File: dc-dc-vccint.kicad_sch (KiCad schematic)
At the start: 53 parts, among them U36 MP8796B, U37 MP8796B

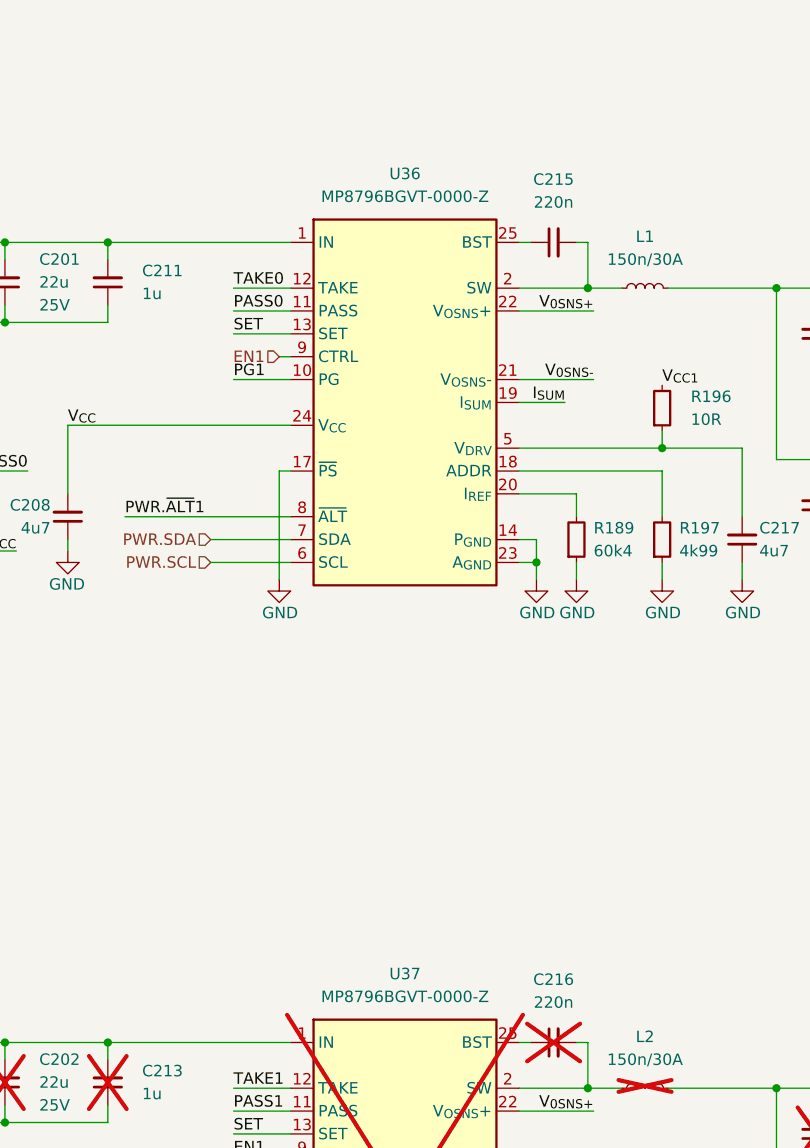
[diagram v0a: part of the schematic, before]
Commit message: [#66727] Update legacy footprints
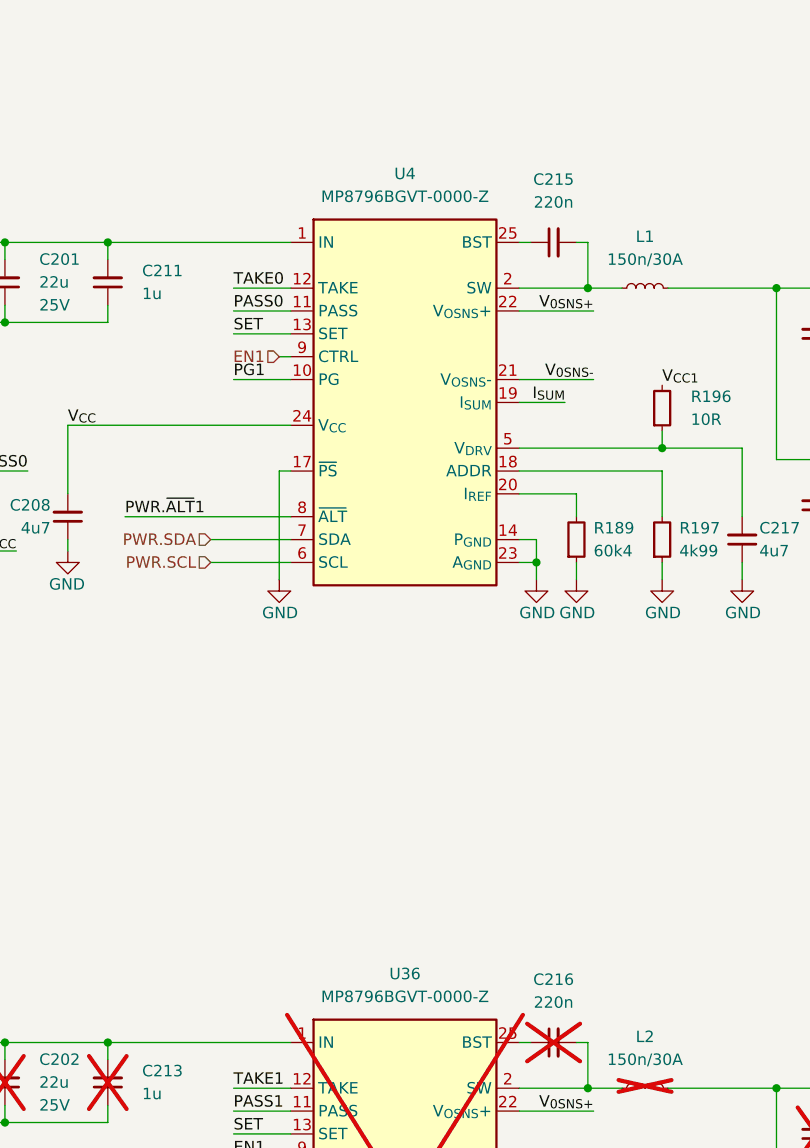
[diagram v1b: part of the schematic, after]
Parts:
- removed U36, U37: MP8796B, symbol antmicroDCDCConverters:MP8796B
- added U36, U4: MP8796B, antmicro-footprints:TQFN-25_4x5mm, symbol DCDCConverters:MP8796B
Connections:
- net EN1: now also U36.9 (CTRL), U4.9 (CTRL)
- net GND: now also U36.14 (P_{GND}), U36.15 (P_{GND}), U36.23 (A_{GND}), U36.4 (P_{GND}), U4.14 (P_{GND}), U4.15 (P_{GND}), U4.17 (~{PS}), U4.23 (A_{GND}), U4.4 (P_{GND})
- net I_{SUM}: now also U36.19 (I_{SUM}), U4.19 (I_{SUM})
- net PASS0: now also U4.11 (PASS)
- net PASS1: now also U36.11 (PASS)
- net PG1: now also U36.10 (PG), U4.10 (PG)
- net PWR.SCL: now also U36.6 (SCL), U4.6 (SCL)
- net PWR.SDA: now also U36.7 (SDA), U4.7 (SDA)
- net PWR.~{ALT}1: now also U4.8 (~{ALT})
- net PWR.~{ALT}2: now also U36.8 (~{ALT})
- net SET: now also U36.13 (SET), U4.13 (SET)
- net TAKE0: now also U4.12 (TAKE)
- net TAKE1: now also U36.12 (TAKE)
- net VDC: now also U36.1 (IN), U36.16 (IN), U4.1 (IN), U4.16 (IN)
- net V_{0SNS+}: now also U36.22 (V_{OSNS}+), U4.22 (V_{OSNS}+)
- net V_{0SNS-}: now also U36.21 (V_{OSNS}-), U4.21 (V_{OSNS}-)
- net V_{CC}: now also U36.24 (V_{CC}), U4.24 (V_{CC})
- net at C218.2, R198.1: now also U36.5 (V_{DRV})
- net at R189.2: now also U4.20 (I_{REF})
- net at R199.2: now also U36.18 (ADDR)
- net at C216.2, L2.1: now also U36.2 (SW), U36.3 (SW)
- net at R195.2: now also U36.20 (I_{REF})
- net at C216.1: now also U36.25 (BST)
- net at C217.2, R196.1: now also U4.5 (V_{DRV})
- net at R197.2: now also U4.18 (ADDR)
- net at C215.1: now also U4.25 (BST)
- net at C215.2, L1.1: now also U4.2 (SW), U4.3 (SW)
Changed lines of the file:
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@@
-    )
-  )
-  (symbol (lib_id "antmicroDCDCConverters:MP8796B") (at 177.8 152.4 0) (unit 1)
-    (in_bom yes) (on_board yes) (dnp yes) (fields_autoplaced)
-    (property "Reference" "U37" (at 190.5 144.78 0)
-      (effects (font (size 1.27 1.27) (thickness 0.15)))
-    )
-    (property "Value" "MP8796B" (at 215.9 162.56 0)
-      (effects (font (size 1.27 1.27) (thickness 0.15)) (justify left bottom) hide)
-    )
-    (property "Footprint" "" (at 215.9 165.1 0)
-      (effects (font (size 1.27 1.27) (thickness 0.15)) (justify left bottom) hide)
-    )
-    (property "Datasheet" "https://www.monolithicpower.com/en/documentview/productdocument/index/version/2/document_type/Datasheet/lang/en/sku/MP8796B/" (at 215.9 167.64 0)
-      (effects (font (size 1.27 1.27) (thickness 0.15)) (justify left bottom) hide)
-    )
-    (property "MPN" "MP8796BGVT-0000-Z" (at 190.5 147.32 0)
-      (effects (font (size 1.27 1.27) (thickness 0.15)))
-    )
-    (property "Manufacturer" "Monolithic Power Systems" (at 215.9 160.02 0)
-      (effects (font (size 1.27 1.27) (thickness 0.15)) (justify left bottom) hide)
-    )
-    (property "Author" "Antmicro" (at 215.9 170.18 0)
-      (effects (font (size 1.27 1.27) (thickness 0.15)) (justify left bottom) hide)
-    )
-    (property "License" "Apache-2.0" (at 215.9 172.72 0)
-      (effects (font (size 1.27 1.27) (thickness 0.15)) (justify left bottom) hide)
-    )
-    (pin "13")
-    (pin "16")
-    (pin "14")
-    (pin "24")
-    (pin "6")
-    (pin "23")
-    (pin "21")
-    (pin "17")
-    (pin "10")
-    (pin "18")
-    (pin "8")
-    (pin "7")
-    (pin "9")
-    (pin "25")
-    (pin "15")
-    (pin "4")
-    (pin "19")
-    (pin "12")
-    (pin "20")
-    (pin "3")
-    (pin "1")
-    (pin "11")
-    (pin "22")
-    (pin "5")
-    (pin "2")
-    (instances
-      (project "data-center-rdimm-ddr5-tester"
-        (path "/1faa6543-e26a-4449-8bac-ee14b9f19e5f/00000000-0000-0000-0000-000060225b0c/3cfc3a6a-24b0-4207-8c35-05eeccc29696"
-          (reference "U37") (unit 1)
-        )
-      )
     )
   )
@@
         (path "/1faa6543-e26a-4449-8bac-ee14b9f19e5f/00000000-0000-0000-0000-000060225b0c/3cfc3a6a-24b0-4207-8c35-05eeccc29696"
           (reference "#PWR0456") (unit 1)
+        )
+      )
+    )
+  )
+  (symbol (lib_id "DCDCConverters:MP8796B") (at 177.8 63.5 0) (unit 1)
+    (in_bom yes) (on_board yes) (dnp no) (fields_autoplaced)
+    (property "Reference" "U4" (at 190.5 55.88 0)
+      (effects (font (size 1.27 1.27) (thickness 0.15)))
+    )
+    (property "Value" "MP8796B" (at 215.9 73.66 0)
+      (effects (font (size 1.27 1.27) (thickness 0.15)) (justify left bottom) hide)
+    )
+    (property "Footprint" "antmicro-footprints:TQFN-25_4x5mm" (at 215.9 76.2 0)
+      (effects (font (size 1.27 1.27) (thickness 0.15)) (justify left bottom) hide)
+    )
+    (property "Datasheet" "https://www.monolithicpower.com/en/documentview/productdocument/index/version/2/document_type/Datasheet/lang/en/sku/MP8796B/" (at 215.9 78.74 0)
+      (effects (font (size 1.27 1.27) (thickness 0.15)) (justify left bottom) hide)
+    )
+    (property "MPN" "MP8796BGVT-0000-Z" (at 190.5 58.42 0)
+      (effects (font (size 1.27 1.27) (thickness 0.15)))
+    )
+    (property "Manufacturer" "Monolithic Power Systems" (at 215.9 71.12 0)
+      (effects (font (size 1.27 1.27) (thickness 0.15)) (justify left bottom) hide)
+    )
+    (property "Author" "Antmicro" (at 215.9 81.28 0)
+      (effects (font (size 1.27 1.27) (thickness 0.15)) (justify left bottom) hide)
+    )
+    (property "License" "Apache-2.0" (at 215.9 83.82 0)
+      (effects (font (size 1.27 1.27) (thickness 0.15)) (justify left bottom) hide)
+    )
+    (pin "7")
+    (pin "8")
+    (pin "16")
+    (pin "5")
+    (pin "6")
+    (pin "10")
+    (pin "22")
+    (pin "9")
+    (pin "11")
+    (pin "13")
+    (pin "1")
+    (pin "14")
+    (pin "19")
+    (pin "23")
+    (pin "21")
+    (pin "3")
+    (pin "4")
+    (pin "2")
+    (pin "24")
+    (pin "17")
+    (pin "18")
+    (pin "15")
+    (pin "20")
+    (pin "12")
+    (pin "25")
+    (instances
+      (project "data-center-rdimm-ddr5-tester"
+        (path "/1faa6543-e26a-4449-8bac-ee14b9f19e5f/00000000-0000-0000-0000-000060225b0c/3cfc3a6a-24b0-4207-8c35-05eeccc29696"
+          (reference "U4") (unit 1)
         )
       )
@@
     )
   )
-  (symbol (lib_id "antmicroDCDCConverters:MP8796B") (at 177.8 63.5 0) (unit 1)
-    (in_bom yes) (on_board yes) (dnp no) (fields_autoplaced)
-    (property "Reference" "U36" (at 190.5 55.88 0)
-      (effects (font (size 1.27 1.27) (thickness 0.15)))
-    )
-    (property "Value" "MP8796B" (at 215.9 73.66 0)
-      (effects (font (size 1.27 1.27) (thickness 0.15)) (justify left bottom) hide)
-    )
-    (property "Footprint" "" (at 215.9 76.2 0)
-      (effects (font (size 1.27 1.27) (thickness 0.15)) (justify left bottom) hide)
-    )
-    (property "Datasheet" "https://www.monolithicpower.com/en/documentview/productdocument/index/version/2/document_type/Datasheet/lang/en/sku/MP8796B/" (at 215.9 78.74 0)
-      (effects (font (size 1.27 1.27) (thickness 0.15)) (justify left bottom) hide)
-    )
-    (property "MPN" "MP8796BGVT-0000-Z" (at 190.5 58.42 0)
-      (effects (font (size 1.27 1.27) (thickness 0.15)))
-    )
-    (property "Manufacturer" "Monolithic Power Systems" (at 215.9 71.12 0)
-      (effects (font (size 1.27 1.27) (thickness 0.15)) (justify left bottom) hide)
-    )
-    (property "Author" "Antmicro" (at 215.9 81.28 0)
-      (effects (font (size 1.27 1.27) (thickness 0.15)) (justify left bottom) hide)
-    )
-    (property "License" "Apache-2.0" (at 215.9 83.82 0)
-      (effects (font (size 1.27 1.27) (thickness 0.15)) (justify left bottom) hide)
-    )
-    (pin "13")
-    (pin "16")
-    (pin "14")
-    (pin "24")
-    (pin "6")
-    (pin "23")
-    (pin "21")
-    (pin "17")
-    (pin "10")
-    (pin "18")
-    (pin "8")
-    (pin "7")
-    (pin "9")
-    (pin "25")
-    (pin "15")
-    (pin "4")
-    (pin "19")
-    (pin "12")
-    (pin "20")
-    (pin "3")
-    (pin "1")
-    (pin "11")
-    (pin "22")
-    (pin "5")
-    (pin "2")
-    (instances
-      (project "data-center-rdimm-ddr5-tester"
-        (path "/1faa6543-e26a-4449-8bac-ee14b9f19e5f/00000000-0000-0000-0000-000060225b0c/3cfc3a6a-24b0-4207-8c35-05eeccc29696"
-          (reference "U36") (unit 1)
-        )
-      )
-    )
-  )
   (symbol (lib_id "antmicropower:+0V85") (at 290.83 60.325 0) (unit 1)
     (in_bom yes) (on_board yes) (dnp no) (fields_autoplaced)
@@
         )
       )
+    )
+  )
+  (symbol (lib_id "DCDCConverters:MP8796B") (at 177.8 152.4 0) (unit 1)
+    (in_bom no) (on_board yes) (dnp yes) (fields_autoplaced)
+    (property "Reference" "U36" (at 190.5 144.78 0)
+      (effects (font (size 1.27 1.27) (thickness 0.15)))
+    )
+    (property "Value" "MP8796B" (at 215.9 162.56 0)
+      (effects (font (size 1.27 1.27) (thickness 0.15)) (justify left bottom) hide)
+    )
+    (property "Footprint" "antmicro-footprints:TQFN-25_4x5mm" (at 215.9 165.1 0)
+      (effects (font (size 1.27 1.27) (thickness 0.15)) (justify left bottom) hide)
+    )
+    (property "Datasheet" "https://www.monolithicpower.com/en/documentview/productdocument/index/version/2/document_type/Datasheet/lang/en/sku/MP8796B/" (at 215.9 167.64 0)
+      (effects (font (size 1.27 1.27) (thickness 0.15)) (justify left bottom) hide)
+    )
+    (property "MPN" "MP8796BGVT-0000-Z" (at 190.5 147.32 0)
+      (effects (font (size 1.27 1.27) (thickness 0.15)))
+    )
+    (property "Manufacturer" "Monolithic Power Systems" (at 215.9 160.02 0)
+      (effects (font (size 1.27 1.27) (thickness 0.15)) (justify left bottom) hide)
+    )
+    (property "Author" "Antmicro" (at 215.9 170.18 0)
+      (effects (font (size 1.27 1.27) (thickness 0.15)) (justify left bottom) hide)
+    )
+    (property "License" "Apache-2.0" (at 215.9 172.72 0)
+      (effects (font (size 1.27 1.27) (thickness 0.15)) (justify left bottom) hide)
+    )
+    (pin "7")
+    (pin "8")
+    (pin "16")
+    (pin "5")
+    (pin "6")
+    (pin "10")
+    (pin "22")
+    (pin "9")
+    (pin "11")
+    (pin "13")
+    (pin "1")
+    (pin "14")
+    (pin "19")
+    (pin "23")
+    (pin "21")
+    (pin "3")
+    (pin "4")
+    (pin "2")
+    (pin "24")
+    (pin "17")
+    (pin "18")
+    (pin "15")
+    (pin "20")
+    (pin "12")
+    (pin "25")
+    (instances
+      (project "data-center-rdimm-ddr5-tester"
+        (path "/1faa6543-e26a-4449-8bac-ee14b9f19e5f/00000000-0000-0000-0000-000060225b0c/3cfc3a6a-24b0-4207-8c35-05eeccc29696"
+          (reference "U36") (unit 1)
+        )
+      )

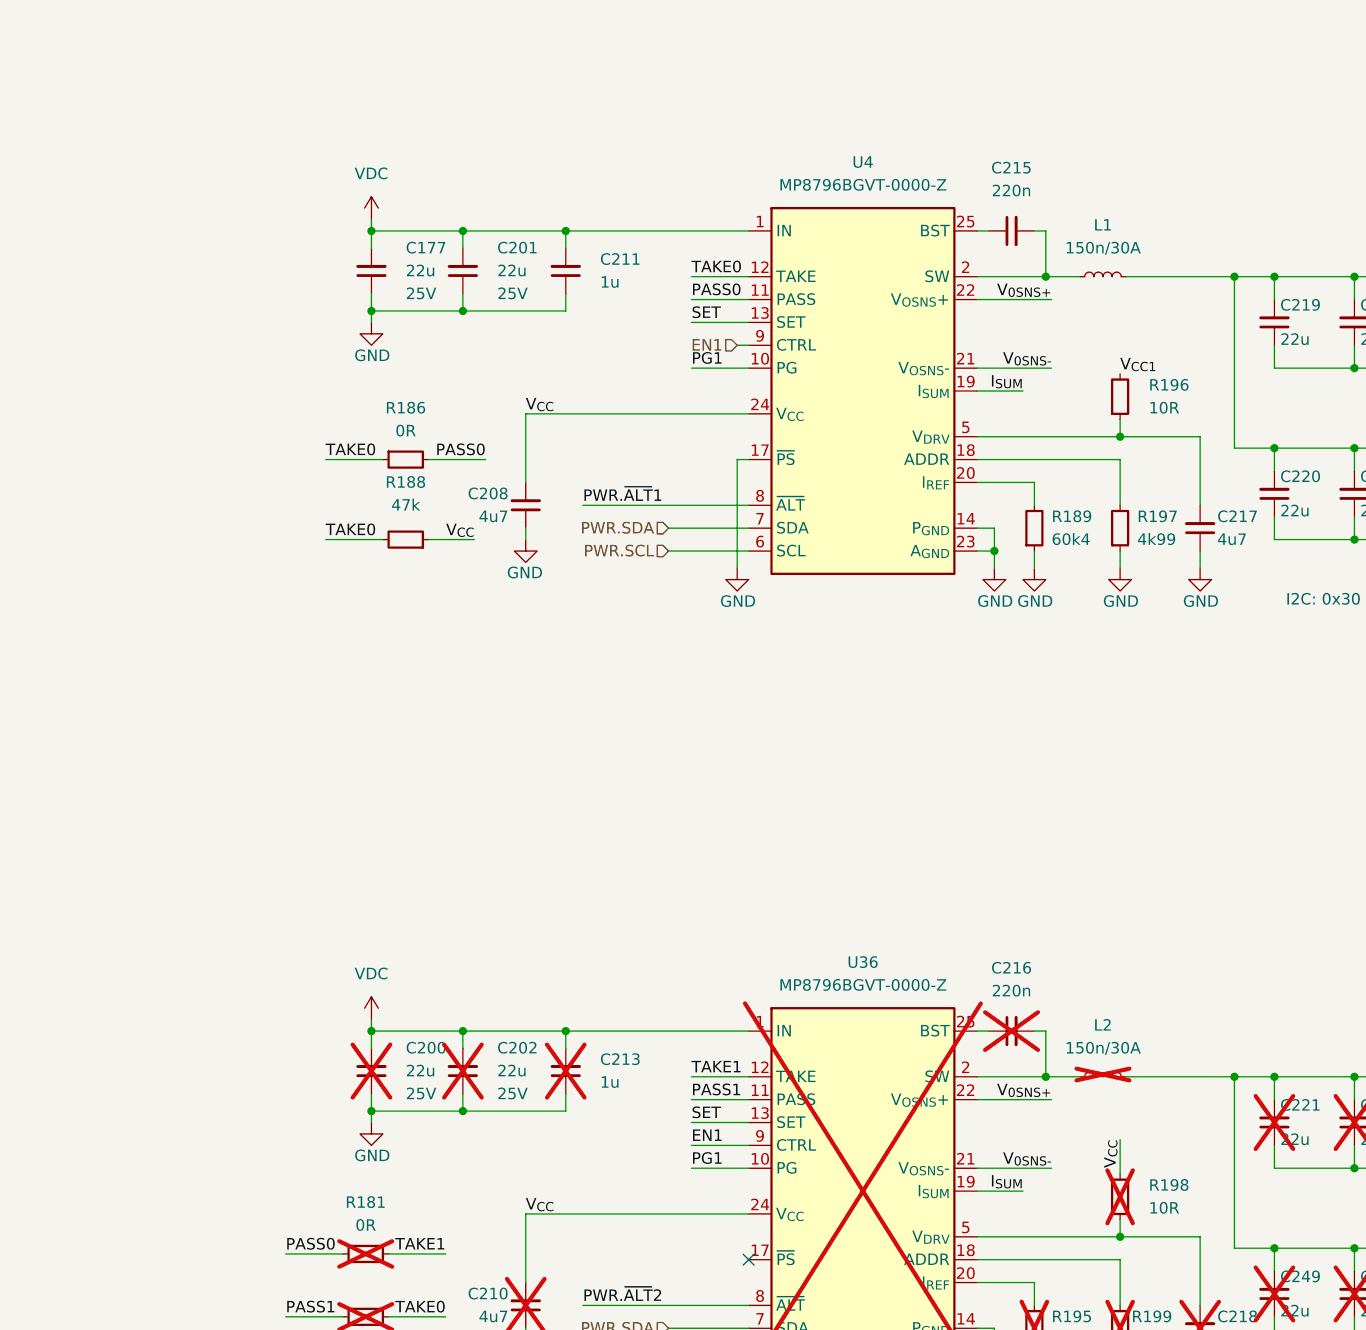
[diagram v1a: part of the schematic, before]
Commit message: [#67115] Add VCCINT input capacitors
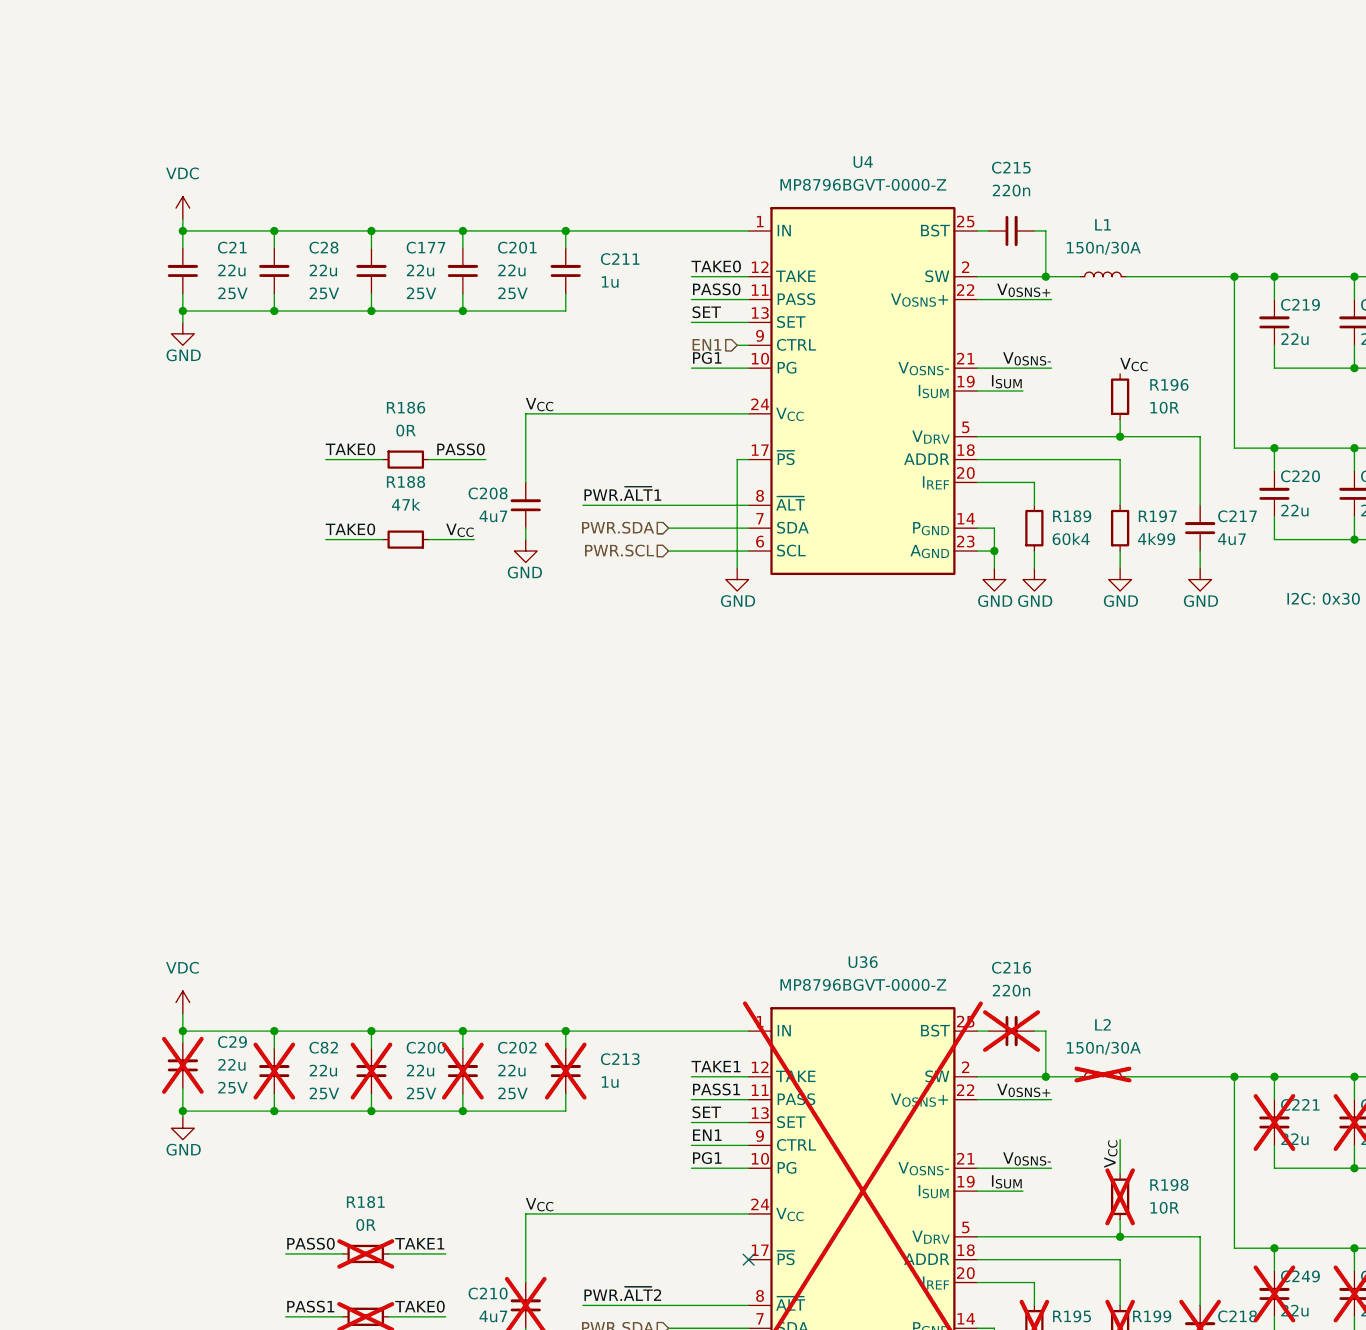
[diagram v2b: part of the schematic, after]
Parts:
- added C21, C28, C29, C82: C_22u_25V_0805, antmicro-footprints:C_0805_2012Metric, symbol antmicroCapacitorsmisc:C_22u_25V_0805
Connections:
- net V_{CC1} is gone; now on net V_{CC}: R196.2
- net GND: now also C21.1, C28.1, C29.1, C82.1
- net VDC: now also C21.2, C28.2, C29.2, C82.2
